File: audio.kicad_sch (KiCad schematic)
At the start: 36 parts, among them IC10 LM386

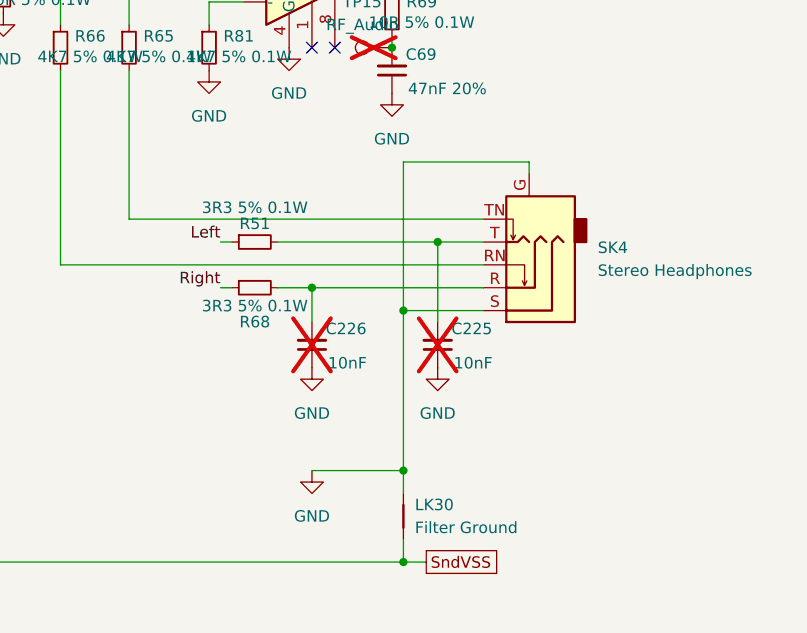
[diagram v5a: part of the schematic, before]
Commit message: change audio jack symbol
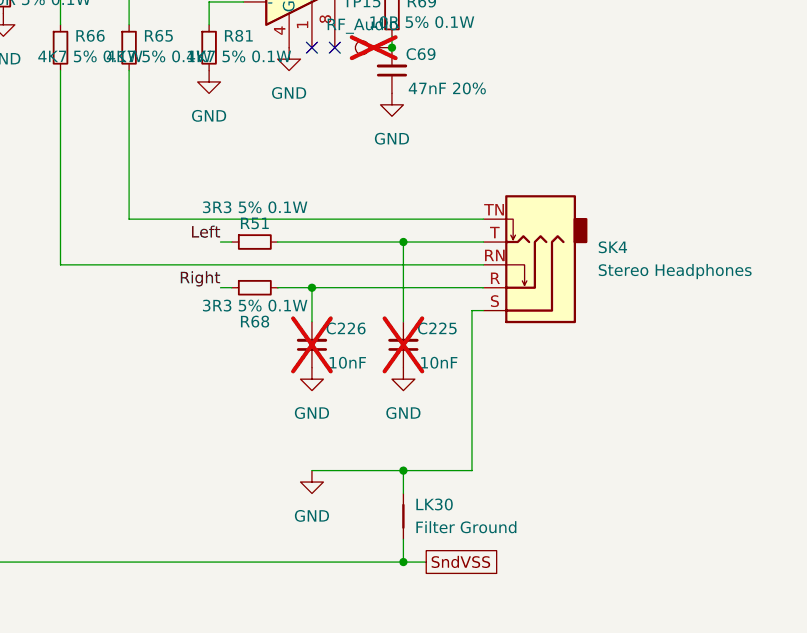
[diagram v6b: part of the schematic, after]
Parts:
- SK4: symbol Connector_Audio:AudioJack3_Ground_SwitchTR -> Connector_Audio:AudioJack3_SwitchTR
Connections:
- net GND: no longer SK4.G
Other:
- moved on the sheet: C225
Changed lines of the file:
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@@
 	)
 	(junction
-		(at 237.49 86.36)
-		(diameter 0)
-		(color 0 0 0 0)
-	)
-	(junction
 		(at 172.72 71.12)
 		(diameter 0)
@@
 	)
 	(junction
-		(at 233.68 93.98)
-		(diameter 0)
-		(color 0 0 0 0)
-	)
-	(junction
 		(at 232.41 64.77)
 		(diameter 0)
@@
 	)
 	(junction
+		(at 233.68 86.36)
+		(diameter 0)
+		(color 0 0 0 0)
+	)
+	(junction
 		(at 128.27 121.92)
 		(diameter 0)
@@
 	(wire
 		(pts
-			(xy 237.49 95.25) (xy 237.49 86.36)
+			(xy 233.68 95.25) (xy 233.68 86.36)
 		)
 		(stroke
@@
 	(wire
 		(pts
-			(xy 237.49 86.36) (xy 242.57 86.36)
-		)
-		(stroke
-			(width 0)
-			(type default)
-		)
-	)
-	(wire
-		(pts
 			(xy 166.37 92.71) (xy 170.18 92.71)
 		)
@@
 	(wire
 		(pts
-			(xy 242.57 93.98) (xy 233.68 93.98)
+			(xy 242.57 93.98) (xy 241.3 93.98)
 		)
 		(stroke
@@
 	(wire
 		(pts
-			(xy 233.68 77.47) (xy 247.65 77.47)
+			(xy 147.32 85.09) (xy 147.32 81.28)
 		)
 		(stroke
@@
 	(wire
 		(pts
-			(xy 147.32 85.09) (xy 147.32 81.28)
+			(xy 139.7 121.92) (xy 132.08 121.92)
 		)
 		(stroke
@@
 	(wire
 		(pts
-			(xy 139.7 121.92) (xy 132.08 121.92)
+			(xy 152.4 121.92) (xy 233.68 121.92)
 		)
 		(stroke
@@
 	(wire
 		(pts
-			(xy 152.4 121.92) (xy 233.68 121.92)
+			(xy 139.7 81.28) (xy 139.7 121.92)
 		)
 		(stroke
@@
 	(wire
 		(pts
-			(xy 139.7 81.28) (xy 139.7 121.92)
+			(xy 233.68 121.92) (xy 236.22 121.92)
 		)
 		(stroke
@@
 	(wire
 		(pts
-			(xy 233.68 121.92) (xy 236.22 121.92)
+			(xy 154.94 81.28) (xy 154.94 92.71)
 		)
 		(stroke
@@
 	(wire
 		(pts
-			(xy 154.94 81.28) (xy 154.94 92.71)
+			(xy 233.68 119.38) (xy 233.68 121.92)
 		)
 		(stroke
@@
 	(wire
 		(pts
-			(xy 233.68 119.38) (xy 233.68 121.92)
+			(xy 241.3 111.76) (xy 233.68 111.76)
 		)
 		(stroke
@@
 	(wire
 		(pts
-			(xy 247.65 77.47) (xy 247.65 78.74)
+			(xy 233.68 86.36) (xy 242.57 86.36)
 		)
 		(stroke
@@
 	(wire
 		(pts
-			(xy 233.68 93.98) (xy 233.68 111.76)
+			(xy 241.3 93.98) (xy 241.3 111.76)
 		)
 		(stroke
@@
 	(wire
 		(pts
-			(xy 233.68 93.98) (xy 233.68 77.47)
-		)
-		(stroke
-			(width 0)
-			(type default)
-		)
-	)
-	(wire
-		(pts
 			(xy 195.58 54.61) (xy 203.2 54.61)
 		)
@@
 	(wire
 		(pts
-			(xy 219.71 86.36) (xy 237.49 86.36)
+			(xy 219.71 86.36) (xy 233.68 86.36)
 		)
 		(stroke
@@
 	(symbol
 		(lib_id "Device:C_Small")
-		(at 237.49 97.79 180)
+		(at 233.68 97.79 180)
 		(unit 1)
 		(exclude_from_sim no)
@@
 		(dnp yes)
 		(property "Reference" "C225"
-			(at 239.014 96.012 0)
+			(at 235.204 96.012 0)
 			(effects
 				(font
@@
 		)
 		(property "Value" "10nF"
-			(at 239.268 99.822 0)
+			(at 235.458 99.822 0)
 			(effects
 				(font
@@
 		)
 		(property "Footprint" "Capacitor_SMD:C_0805_2012Metric"
-			(at 237.49 97.79 0)
+			(at 233.68 97.79 0)
 			(effects
 				(font
@@
 		)
 		(property "Datasheet" "~"
-			(at 237.49 97.79 0)
+			(at 233.68 97.79 0)
 			(effects
 				(font
@@
 		)
 		(property "Description" "Unpolarized capacitor, small symbol"
-			(at 237.49 97.79 0)
+			(at 233.68 97.79 0)
 			(effects
 				(font
@@
 		)
 		(property "LCSC" "C83170"
-			(at 237.49 97.79 0)
+			(at 233.68 97.79 0)
 			(effects
 				(font
@@
 		)
 		(property "LCSC Part" "C83170"
-			(at 237.49 97.79 0)
+			(at 233.68 97.79 0)
 			(effects
 				(font
@@
 	(symbol
 		(lib_id "power:GND")
-		(at 237.49 100.33 0)
+		(at 233.68 100.33 0)
 		(unit 1)
 		(exclude_from_sim no)
@@
 		(fields_autoplaced yes)
 		(property "Reference" "#PWR0339"
-			(at 237.49 106.68 0)
+			(at 233.68 106.68 0)
 			(effects
 				(font
@@
 		)
 		(property "Value" "GND"
-			(at 237.49 105.41 0)
+			(at 233.68 105.41 0)
 			(effects
 				(font
@@
 		)
 		(property "Footprint" ""
-			(at 237.49 100.33 0)
+			(at 233.68 100.33 0)
 			(effects
 				(font
@@
 		)
 		(property "Datasheet" ""
-			(at 237.49 100.33 0)
+			(at 233.68 100.33 0)
 			(effects
 				(font
@@
 		)
 		(property "Description" "Power symbol creates a global label with name \"GND\" , ground"
-			(at 237.49 100.33 0)
+			(at 233.68 100.33 0)
 			(effects
 				(font
@@
 	)
 	(symbol
-		(lib_id "Connector_Audio:AudioJack3_Ground_SwitchTR")
+		(lib_id "Connector_Audio:AudioJack3_SwitchTR")
 		(at 247.65 91.44 180)
 		(unit 1)
@@
 			)
 		)
-		(property "Description" "Audio Jack, 3 Poles (Stereo / TRS), Grounded Sleeve, Switched TR Poles (Normalling)"
+		(property "Description" "Audio Jack, 3 Poles (Stereo / TRS), Switched TR Poles (Normalling)"
 			(at 247.65 91.44 0)
 			(effects
@@
 		(pin "TN"
 		)
-		(pin "G"
-		)
 		(pin "S"
